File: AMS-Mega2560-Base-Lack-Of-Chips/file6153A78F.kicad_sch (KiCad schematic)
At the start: 21 parts, among them IC7 LTV-846S, Q1 2N7000, Q2 2N7000, Q3 2N7000, Q4 2N7000

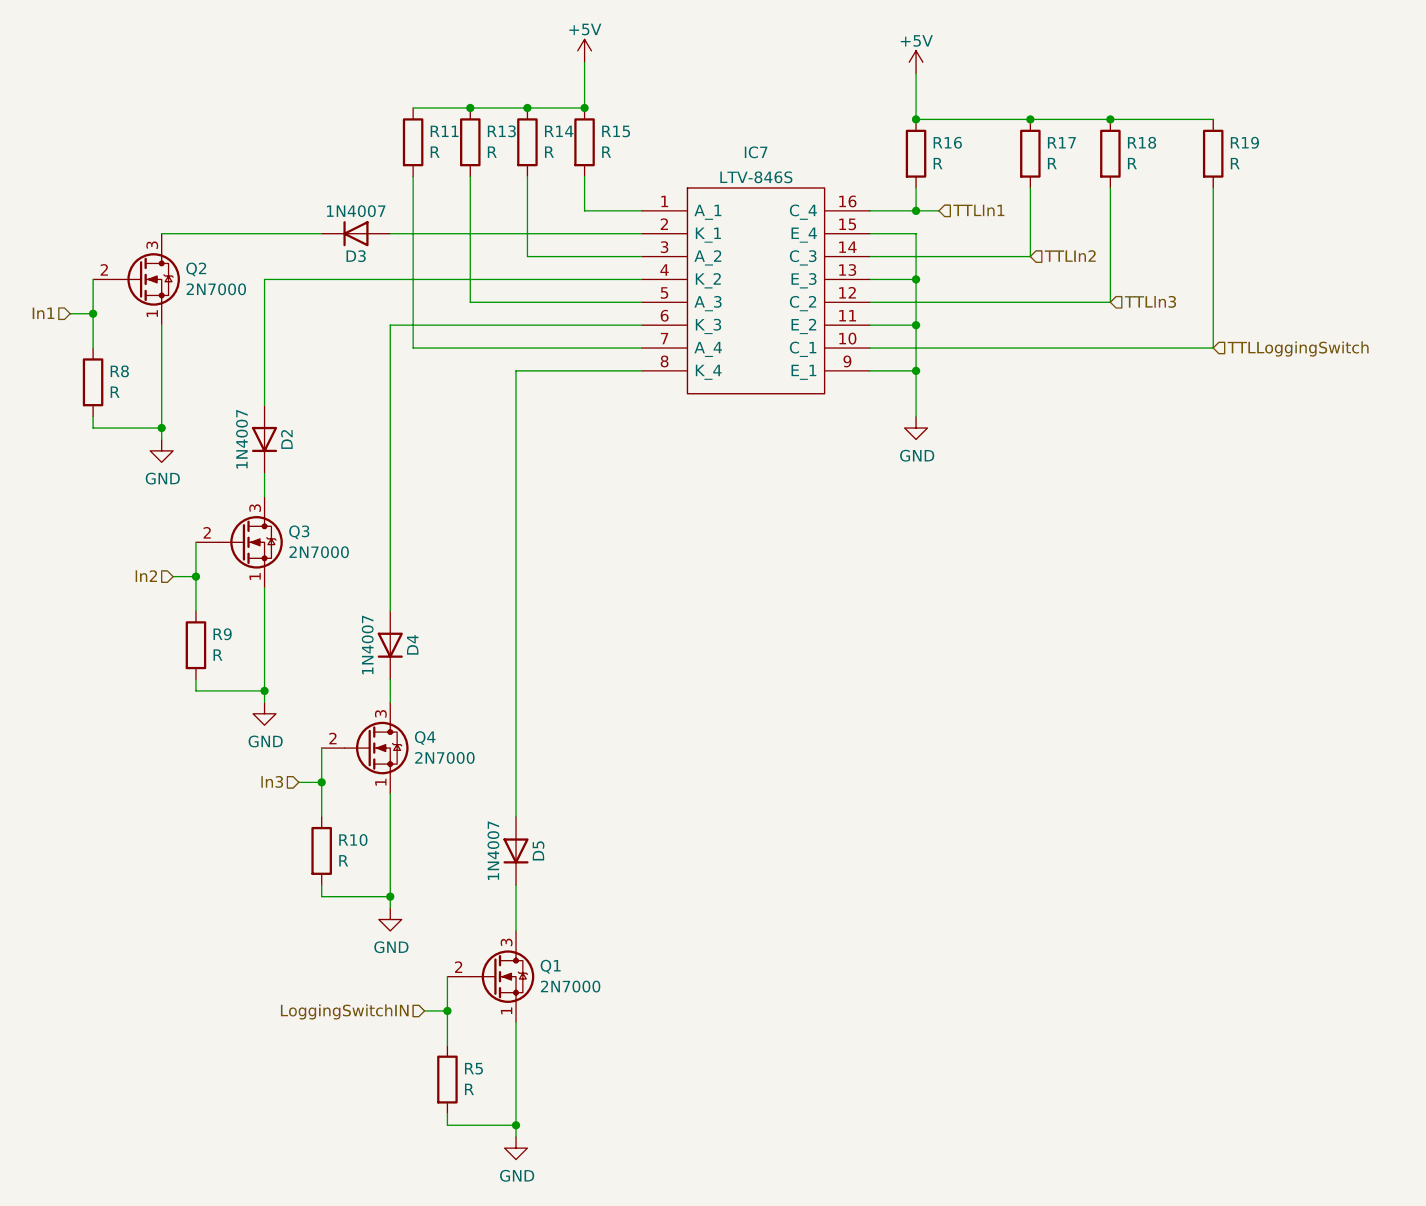
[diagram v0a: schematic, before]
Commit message: updating some Resistor values
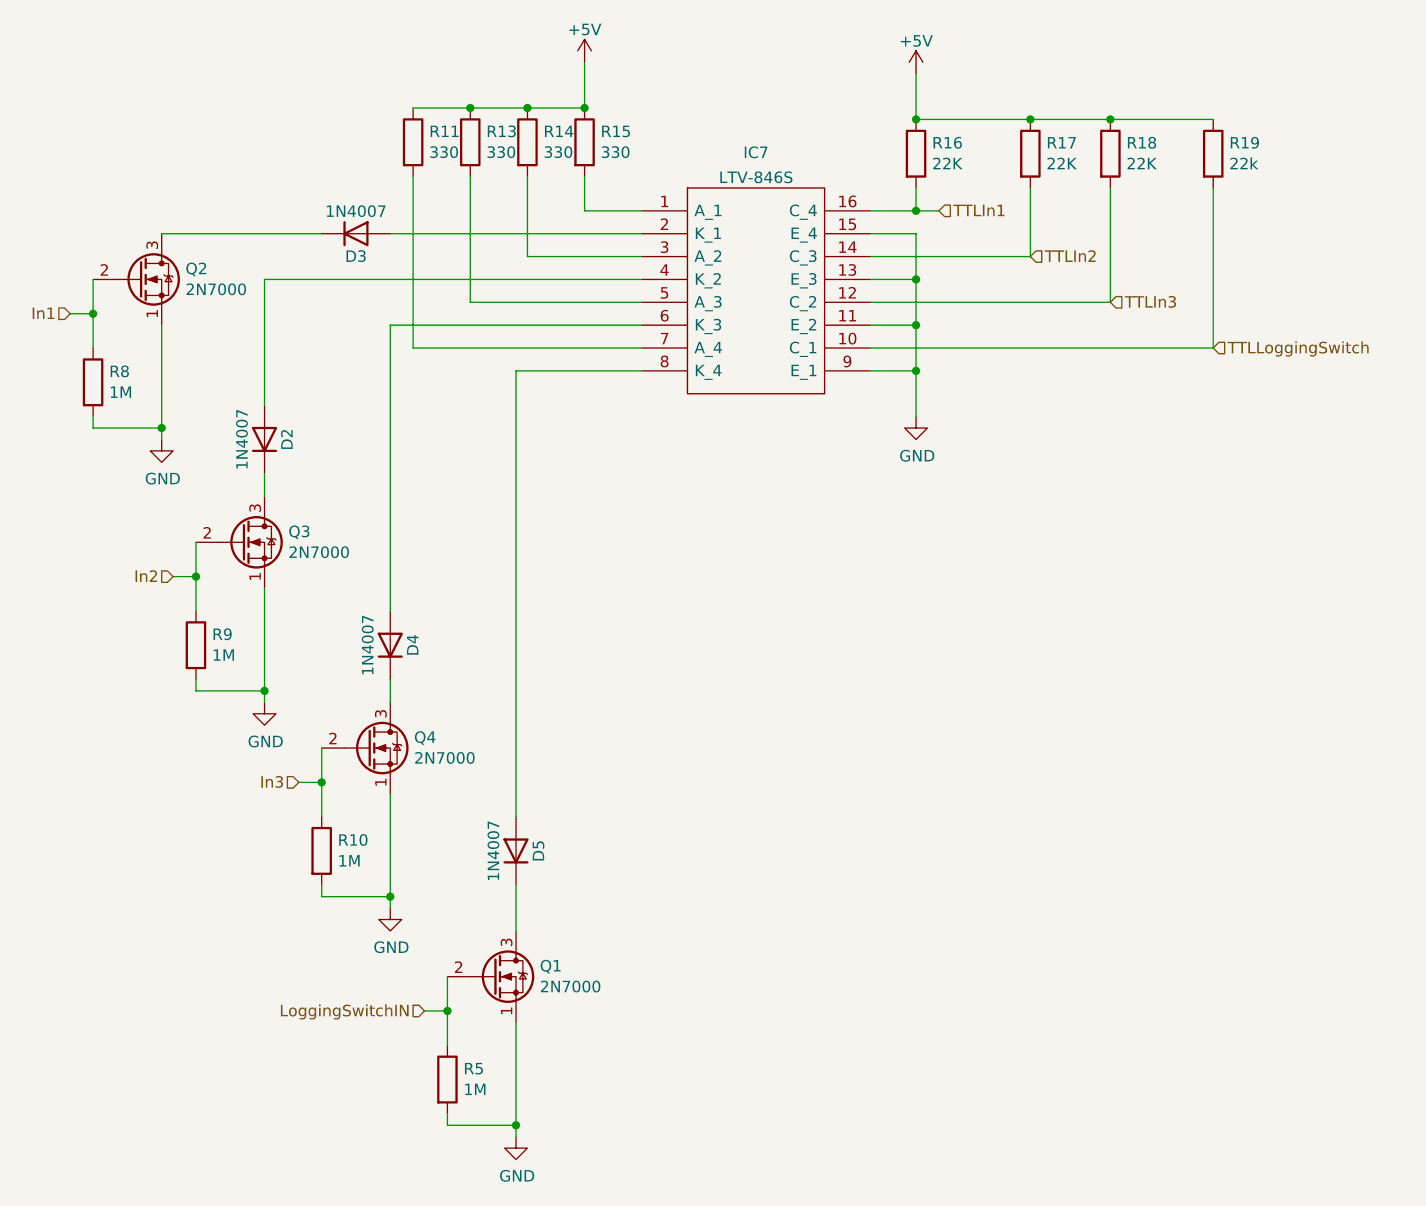
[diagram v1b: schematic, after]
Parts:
- R10, R5, R8, R9: value R -> 1M
- R11, R13, R14, R15: value R -> 330
- R16, R17, R18: value R -> 22K
- R19: value R -> 22k
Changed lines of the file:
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@@
       (effects (font (size 1.27 1.27)) (justify left))
     )
-    (property "Value" "R" (id 1) (at 241.808 39.243 0)
+    (property "Value" "22K" (id 1) (at 241.808 39.243 0)
       (effects (font (size 1.27 1.27)) (justify left))
     )
@@
       (effects (font (size 1.27 1.27)) (justify left))
     )
-    (property "Value" "R" (id 1) (at 149.098 93.853 0)
+    (property "Value" "1M" (id 1) (at 149.098 93.853 0)
       (effects (font (size 1.27 1.27)) (justify left))
     )
@@
       (effects (font (size 1.27 1.27)) (justify left))
     )
-    (property "Value" "R" (id 1) (at 192.278 37.973 0)
+    (property "Value" "330" (id 1) (at 192.278 37.973 0)
       (effects (font (size 1.27 1.27)) (justify left))
     )
@@
       (effects (font (size 1.27 1.27)) (justify left))
     )
-    (property "Value" "R" (id 1) (at 137.668 64.643 0)
+    (property "Value" "1M" (id 1) (at 137.668 64.643 0)
       (effects (font (size 1.27 1.27)) (justify left))
     )
@@
       (effects (font (size 1.27 1.27)) (justify left))
     )
-    (property "Value" "R" (id 1) (at 185.928 37.973 0)
+    (property "Value" "330" (id 1) (at 185.928 37.973 0)
       (effects (font (size 1.27 1.27)) (justify left))
     )
@@
       (effects (font (size 1.27 1.27)) (justify left))
     )
-    (property "Value" "R" (id 1) (at 179.578 37.973 0)
+    (property "Value" "330" (id 1) (at 179.578 37.973 0)
       (effects (font (size 1.27 1.27)) (justify left))
     )
@@
       (effects (font (size 1.27 1.27)) (justify left))
     )
-    (property "Value" "R" (id 1) (at 229.108 39.243 0)
+    (property "Value" "22K" (id 1) (at 229.108 39.243 0)
       (effects (font (size 1.27 1.27)) (justify left))
     )
@@
       (effects (font (size 1.27 1.27)) (justify left))
     )
-    (property "Value" "R" (id 1) (at 250.698 39.243 0)
+    (property "Value" "22K" (id 1) (at 250.698 39.243 0)
       (effects (font (size 1.27 1.27)) (justify left))
     )
@@
       (effects (font (size 1.27 1.27)) (justify left))
     )
-    (property "Value" "R" (id 1) (at 173.228 37.973 0)
+    (property "Value" "330" (id 1) (at 173.228 37.973 0)
       (effects (font (size 1.27 1.27)) (justify left))
     )
@@
       (effects (font (size 1.27 1.27)) (justify left))
     )
-    (property "Value" "R" (id 1) (at 262.128 39.243 0)
+    (property "Value" "22k" (id 1) (at 262.128 39.243 0)
       (effects (font (size 1.27 1.27)) (justify left))
     )
@@
       (effects (font (size 1.27 1.27)) (justify left))
     )
-    (property "Value" "R" (id 1) (at 163.068 116.713 0)
+    (property "Value" "1M" (id 1) (at 163.068 116.713 0)
       (effects (font (size 1.27 1.27)) (justify left))
     )
@@
       (effects (font (size 1.27 1.27)) (justify left))
     )
-    (property "Value" "R" (id 1) (at 177.038 142.113 0)
-      (effects (font (size 1.27 1.27)) (justify left))
-    )
+    (property "Value" "1M" (id 1) (at 177.038 142.113 0)
+      (effects (font (size 1.27 1.27)) (justify left))
+    )
